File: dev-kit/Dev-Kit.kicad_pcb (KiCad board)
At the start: 4 copper layers, 110 x 70 mm, 118 parts, among them IC101 nPM1300-QEXX, IC201 APDS-9306-065, IC202 RV-8263-C8, IC203 BMI270, IC204 LIS2MDLTR, IC205 BMP581, IC206 DRV2603RUNT, IC301 FAN5622SX, IC302 MX25U51245GZ4I00, IC303 USBLC6-2P6, IC304 NTS0104GU12, M301 NORA-B106, Q201 DMG1013UW-7, Q202 PMZ550UNEYL, Q203 PMZ550UNEYL, X101 Battery, X102 Battery, X103 Power, X201 Power, X202 I2S, X203 Power, X204 I2C, X205 Power, X206 Power, X207 Power, X208 Power, X209 Power, X210 Motor, X301 Power, X302 Power, X303 Device, X304 UART, X305 IO Power, X306 Display, X307 Touch Power, X308 LED Power, X309 DEBUG, X310 GPIO

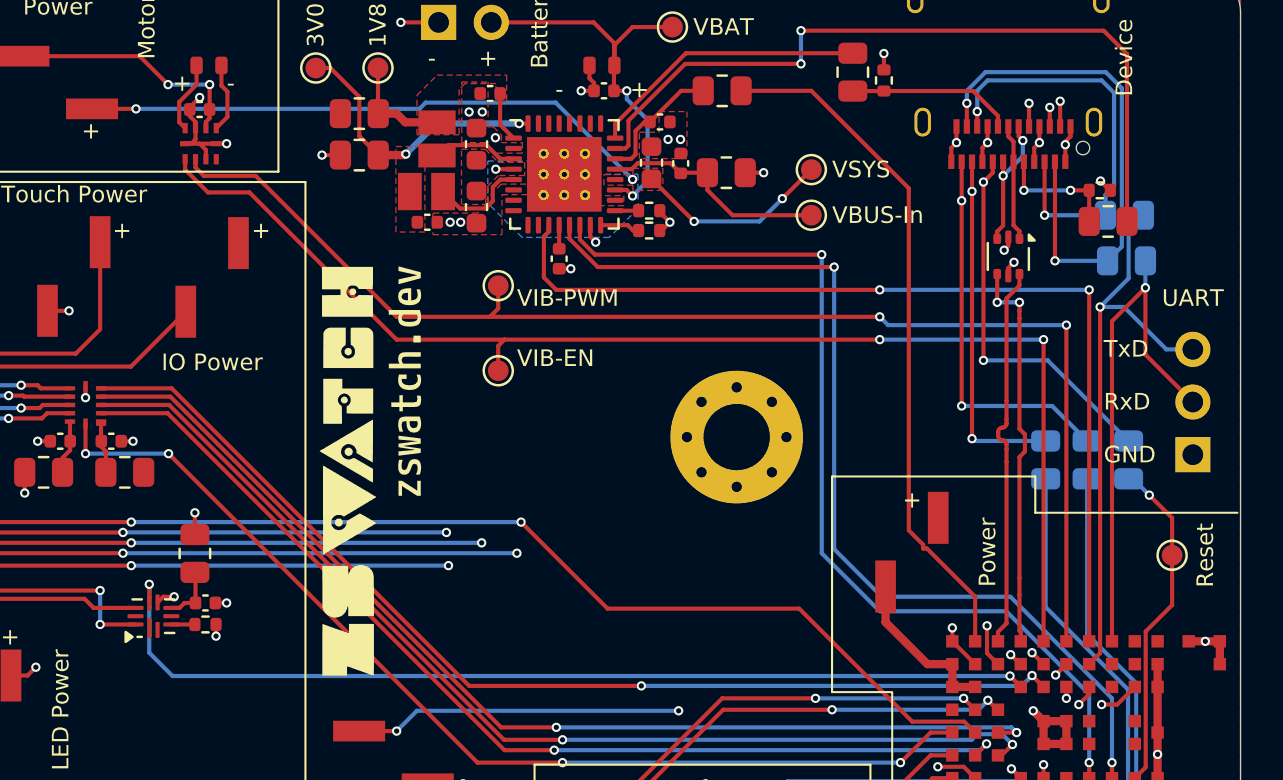
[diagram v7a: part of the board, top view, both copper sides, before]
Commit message: Add impedance matching for USB, add jumper caps
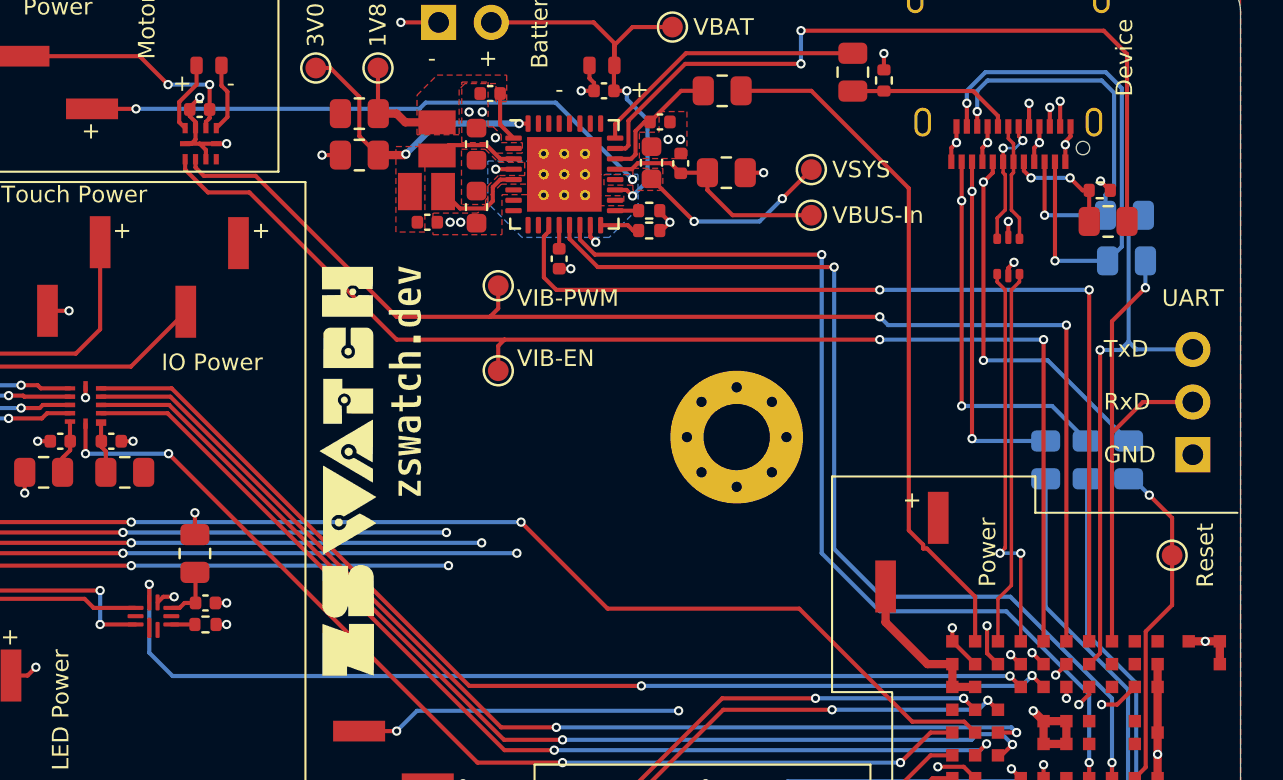
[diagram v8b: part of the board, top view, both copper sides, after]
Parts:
- turned R301 to 0 degrees
- renumbered X310 to X304, X304 to X305, X305 to X306, X306 to X307, X307 to X308, X308 to X309, X309 to X310
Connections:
- net Net-(IC303-I/O1-Pad1) renamed /MCU/D+
- net Net-(IC303-I/O2-Pad3) renamed /MCU/D-
- R301 pad 1: GND -> Net-(IC301-ISET)
- R301 pad 2: Net-(IC301-ISET) -> GND
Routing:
- net RxD: track 25.8 -> 23.9 mm
- net TxD: track 28.5 -> 26.9 mm
- net Net-(X303-CC1): track 6.03 -> 5.48 mm
